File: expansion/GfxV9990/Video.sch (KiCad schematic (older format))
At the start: 1 part

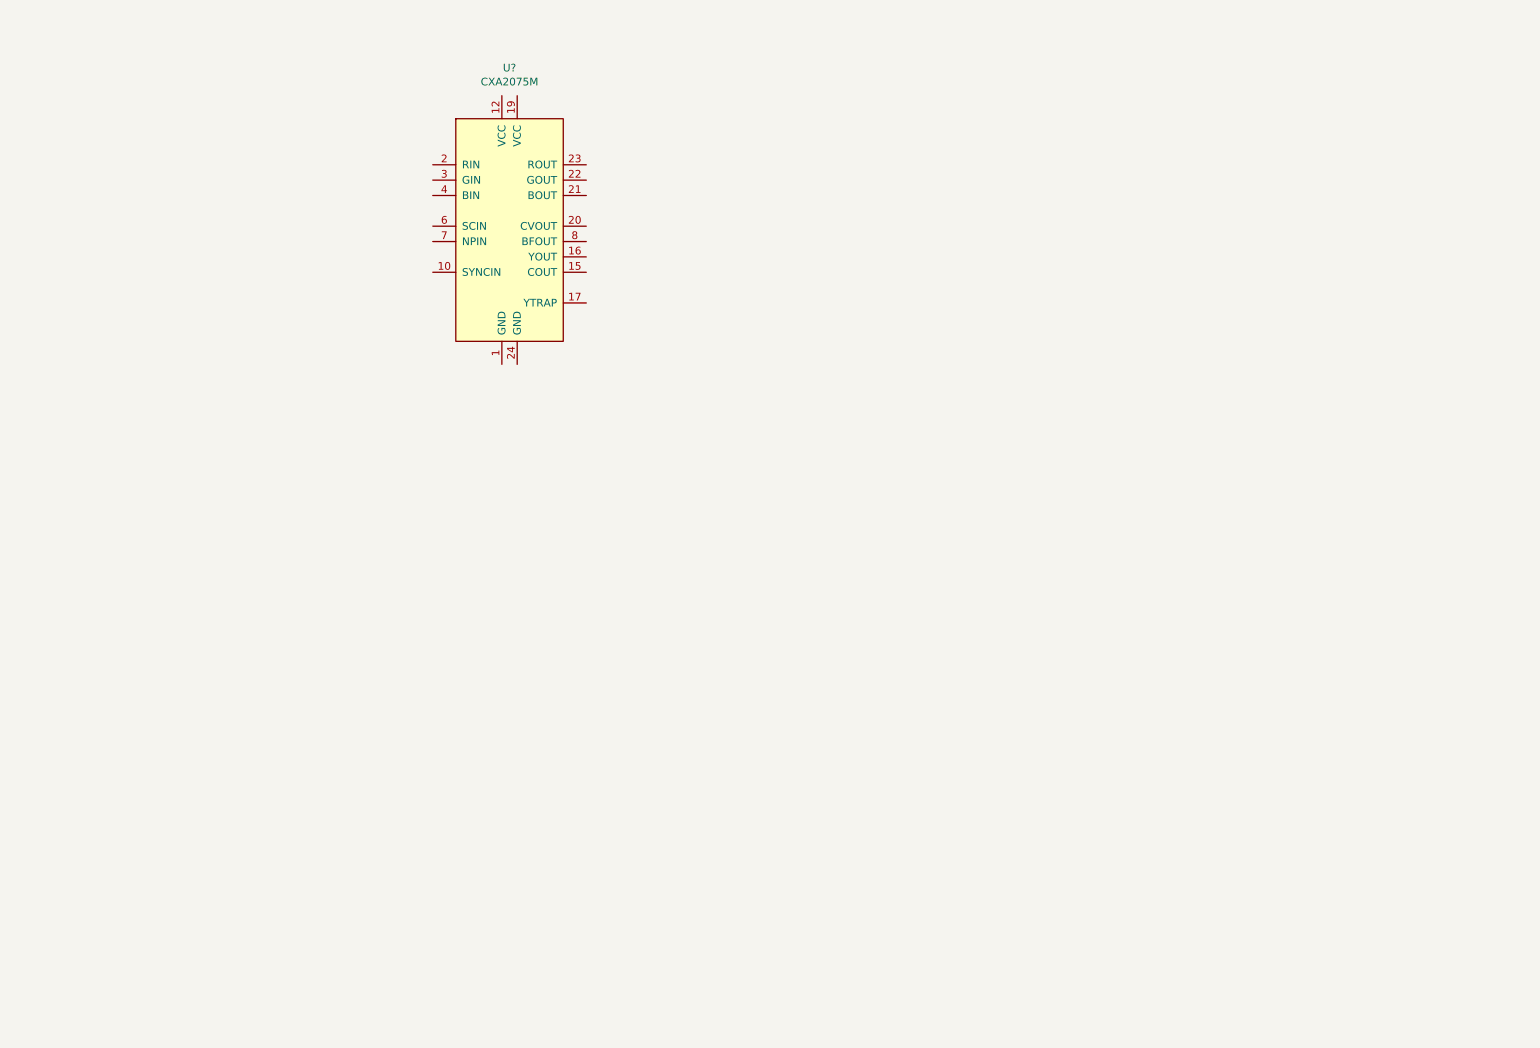
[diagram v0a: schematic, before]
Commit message: More additions to the V9990
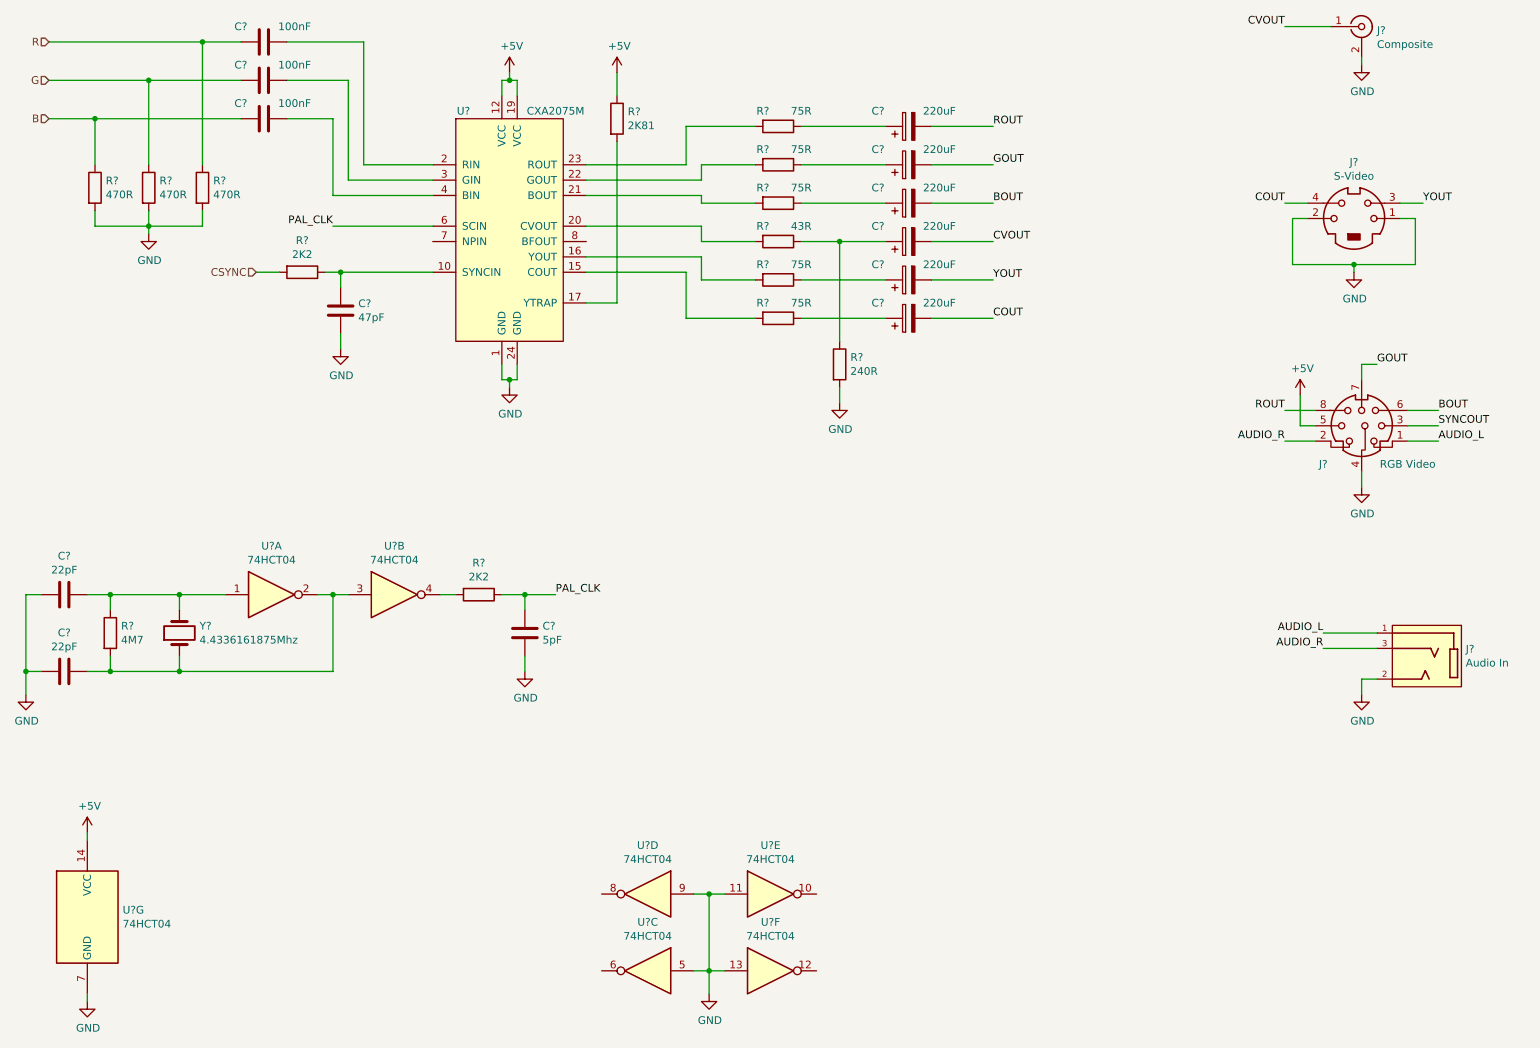
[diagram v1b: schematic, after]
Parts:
- added C? (x6): 220uF, symbol Device:CP
- added C?: 47pF, symbol Device:C
- added C? (x2): 22pF, symbol Device:C
- added C?: 5pF, symbol Device:C
- added C? (x3): 100nF, symbol Device:C
- added J?: RGB Video, symbol Connector:Mini-DIN-8
- added J?: S-Video, symbol Connector:Mini-DIN-4
- added J?: Composite, symbol Connector:Conn_Coaxial
- added J?: Audio In, SWITCHCRAFT_35RAPC2BHN2, symbol Ddraig:35RAPC2BHN2
- added R?: 2K81, symbol Device:R
- added R? (x5): 75R, symbol Device:R
- added R?: 43R, symbol Device:R
- added R?: 240R, symbol Device:R
- added R? (x2): 2K2, symbol Device:R
- added R?: 4M7, symbol Device:R
- added R? (x3): 470R, symbol Device:R
- added U? (x7): 74HCT04, symbol 74xx:74HCT04
- added Y?: 4.4336161875Mhz, symbol Device:Crystal
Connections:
- net GND: now reaches U?.1 (GND)
- net GND: now also U?.24 (GND), C?.2, C?.2, C?.2, C?.2, J?.1, J?.2, J?.2, J?.2 (Ext), J?.4, R?.2, R?.2, R?.2, R?.2, U?.11, U?.13, U?.5, U?.7 (GND), U?.9
- net at U?.10 (SYNCIN): now also C?.1, R?.1
- net +5V: now reaches U?.12 (VCC)
- net +5V: now also U?.19 (VCC), J?.5, R?.1, U?.14 (VCC)
- net at U?.15 (COUT): now also R?.2
- net at U?.16 (YOUT): now also R?.2
- net at U?.17 (YTRAP): now also R?.2
- net at U?.2 (RIN): now also C?.1
- net at U?.20 (CVOUT): now also R?.2
- net at U?.21 (BOUT): now also R?.2
- net at U?.22 (GOUT): now also R?.2
- net at U?.23 (ROUT): now also R?.2
- net at U?.3 (GIN): now also C?.1
- net at U?.4 (BIN): now also C?.1
- net PAL_CLK: now reaches U?.6 (SCIN)
- net PAL_CLK: now also C?.1, R?.1
- new net: C?.1, R?.1 (x5)
- new net: C?.1, R?.1, R?.1
- new net: C?.1, R?.1, U?.1, Y?.2
- new net: C?.1, R?.2, U?.2, U?.3, Y?.1
- new net: R?.2, U?.4
- new net AUDIO_L: J?.1, J?.1
- new net AUDIO_R: J?.2, J?.3
- new net B: C?.2, R?.1
- new net BOUT: C?.2, J?.6
- new net COUT: C?.2, J?.4
- new net CSYNC: R?.2
- new net CVOUT: C?.2, J?.1 (In)
- new net G: C?.2, R?.1
- new net GOUT: C?.2, J?.7
- new net R: C?.2, R?.1
- new net ROUT: C?.2, J?.8
- new net SYNCOUT: J?.3
- new net YOUT: C?.2, J?.3

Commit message: Added V9958 board
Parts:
- added C18: 220uF, symbol Device:CP
- added Q1: 2N3904, Package_TO_SOT_THT:TO-92_Inline, symbol Transistor_BJT:2N3904
- added R23, R24: R, symbol Device:R
- added R25: 220R, symbol Device:R
- J6: renamed from J?; footprint SWITCHCRAFT_35RAPC2BHN2 -> Ddraig:SWITCHCRAFT_35RAPC2BHN2
- gave numbers to parts that had none: 33
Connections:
- net +5V: now also Q1.3 (C)
- net CSYNC: now also R23.2
- net GND: now also R24.2
- net SYNCOUT: now also R25.1
- new net: Q1.2 (B), R23.1
- new net: C18.1, Q1.1 (E), R24.1
- new net: C18.2, R25.2
- no-connect marks 0 -> 6

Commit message: Added Eth8019 and updated page description for all projects
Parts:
- added C? (x3): 100nF, symbol Device:C
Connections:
- net +5V: now also C?.1, C?.1, C?.1
- net GND: now also C?.2, C?.2, C?.2
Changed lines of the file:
@@
 Wire Wire Line
 	8250 5150 8150 5150
+$Comp
+L Device:C C?
+U 1 1 60F7C479
+P 3400 6850
+F 0 "C?" H 3515 6896 50  0000 L CNN
+F 1 "100nF" H 3515 6805 50  0000 L CNN
+F 2 "" H 3438 6700 50  0001 C CNN
+F 3 "~" H 3400 6850 50  0001 C CNN
+	1    3400 6850
+	1    0    0    -1
+$EndComp
+$Comp
+L Device:C C?
+U 1 1 60F7C47F
+P 3850 6850
+F 0 "C?" H 3965 6896 50  0000 L CNN
+F 1 "100nF" H 3965 6805 50  0000 L CNN
+F 2 "" H 3888 6700 50  0001 C CNN
+F 3 "~" H 3850 6850 50  0001 C CNN
+	1    3850 6850
+	1    0    0    -1
+$EndComp
+$Comp
+L Device:C C?
+U 1 1 60F7C485
+P 2900 6850
+F 0 "C?" H 3015 6896 50  0000 L CNN
+F 1 "100nF" H 3015 6805 50  0000 L CNN
+F 2 "" H 2938 6700 50  0001 C CNN
+F 3 "~" H 2900 6850 50  0001 C CNN
+	1    2900 6850
+	1    0    0    -1
+$EndComp
+$Comp
+L power:GND #PWR?
+U 1 1 60F7C48B
+P 3400 7150
+F 0 "#PWR?" H 3400 6900 50  0001 C CNN
+F 1 "GND" H 3405 6977 50  0000 C CNN
+F 2 "" H 3400 7150 50  0001 C CNN
+F 3 "" H 3400 7150 50  0001 C CNN
+	1    3400 7150
+	1    0    0    -1
+$EndComp
+$Comp
+L power:+5V #PWR?
+U 1 1 60F7C491
+P 3400 6500
+F 0 "#PWR?" H 3400 6350 50  0001 C CNN
+F 1 "+5V" H 3415 6673 50  0000 C CNN
+F 2 "" H 3400 6500 50  0001 C CNN
+F 3 "" H 3400 6500 50  0001 C CNN
+	1    3400 6500
+	1    0    0    -1
+$EndComp
+Wire Wire Line
+	2900 6700 2900 6600
+Wire Wire Line
+	2900 6600 3400 6600
+Wire Wire Line
+	3850 6600 3850 6700
+Wire Wire Line
+	3400 6700 3400 6600
+Connection ~ 3400 6600
+Wire Wire Line
+	3400 6600 3850 6600
+Wire Wire Line
+	3400 6600 3400 6500
+Wire Wire Line
+	2900 7000 2900 7100
+Wire Wire Line
+	2900 7100 3400 7100
+Wire Wire Line
+	3850 7100 3850 7000
+Wire Wire Line
+	3400 7000 3400 7100
+Connection ~ 3400 7100
+Wire Wire Line
+	3400 7100 3850 7100
+Wire Wire Line
+	3400 7150 3400 7100
 $EndSCHEMATC

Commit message: Started work on V9990 PCB layout
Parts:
- C13: renamed from C5; footprint (none) -> Capacitor_SMD:C_0805_2012Metric
- C14: renamed from C6; footprint (none) -> Capacitor_SMD:C_0805_2012Metric
- C15: renamed from C7; footprint (none) -> Capacitor_SMD:C_0805_2012Metric
- C16: renamed from C8; footprint (none) -> Capacitor_SMD:C_0805_2012Metric
- C17: renamed from C9; footprint (none) -> Capacitor_SMD:C_0805_2012Metric
- C18, C20, C21: renamed from C?; footprint (none) -> Capacitor_SMD:C_0805_2012Metric
- C19: renamed from C10; footprint (none) -> Capacitor_SMD:C_0805_2012Metric
- C22: renamed from C11; footprint (none) -> Capacitor_SMD:C_0805_2012Metric
- C23: renamed from C12; footprint (none) -> Capacitor_SMD:CP_Elec_6.3x5.8
- C24: renamed from C13; footprint (none) -> Capacitor_SMD:CP_Elec_6.3x5.8
- C25: renamed from C14; footprint (none) -> Capacitor_SMD:CP_Elec_6.3x5.8
- C26: renamed from C15; footprint (none) -> Capacitor_SMD:CP_Elec_6.3x5.8
- C27: renamed from C16; footprint (none) -> Capacitor_SMD:CP_Elec_6.3x5.8
- C28: renamed from C17; footprint (none) -> Capacitor_SMD:CP_Elec_6.3x5.8
- C29: renamed from C18; footprint (none) -> Capacitor_SMD:CP_Elec_6.3x5.8
- J3: footprint (none) -> Ddraig:TE_5749181-1
- J4: footprint (none) -> Ddraig:KLPX0848A2RG
- J5: footprint (none) -> Ddraig:TE_57492681
- R10: renamed from R11; footprint (none) -> Inductor_SMD:L_0805_2012Metric
- R11: renamed from R12; footprint (none) -> Inductor_SMD:L_0805_2012Metric
- R12: renamed from R13; footprint (none) -> Inductor_SMD:L_0805_2012Metric
- R13: renamed from R14; footprint (none) -> Inductor_SMD:L_0805_2012Metric
- R14: renamed from R15; footprint (none) -> Inductor_SMD:L_0805_2012Metric
- R15: renamed from R16; footprint (none) -> Inductor_SMD:L_0805_2012Metric
- R16: renamed from R17; footprint (none) -> Inductor_SMD:L_0805_2012Metric
- R17: renamed from R18; footprint (none) -> Inductor_SMD:L_0805_2012Metric
- R18: renamed from R19; footprint (none) -> Inductor_SMD:L_0805_2012Metric
- R19: renamed from R20; footprint (none) -> Inductor_SMD:L_0805_2012Metric
- R20: renamed from R21; footprint (none) -> Inductor_SMD:L_0805_2012Metric
- R21: renamed from R22; footprint (none) -> Inductor_SMD:L_0805_2012Metric
- R22: renamed from R23; value R -> 1K; footprint (none) -> Inductor_SMD:L_0805_2012Metric
- R23: renamed from R24; value R -> 100R; footprint (none) -> Inductor_SMD:L_0805_2012Metric
- R24: renamed from R25; footprint (none) -> Inductor_SMD:L_0805_2012Metric
- R8: renamed from R9; footprint (none) -> Inductor_SMD:L_0805_2012Metric
- R9: renamed from R10; footprint (none) -> Inductor_SMD:L_0805_2012Metric
- U6: footprint (none) -> Package_SO:SO-14_5.3x10.2mm_P1.27mm
- Y2: footprint (none) -> Crystal:Crystal_HC50_Vertical

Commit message: Working on video board
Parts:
- removed Q1: 2N3904, Package_TO_SOT_THT:TO-92_Inline, symbol Transistor_BJT:2N3904
- added Q1: BC817, Package_TO_SOT_SMD:SOT-23, symbol Transistor_BJT:BC817
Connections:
- net +5V: now also Q1.3 (C)
- net at R22.1: now also Q1.1 (B)
- net at C29.1, R23.1: now also Q1.2 (E)
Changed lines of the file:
@@
-$EndComp
-$Comp
-L Transistor_BJT:2N3904 Q1
-U 1 1 60EAD7FF
-P 7000 4750
-F 0 "Q1" H 7190 4796 50  0000 L CNN
-F 1 "2N3904" H 7190 4705 50  0000 L CNN
-F 2 "Package_TO_SOT_THT:TO-92_Inline" H 7200 4675 50  0001 L CIN
-F 3 "https://www.onsemi.com/pub/Collateral/2N3903-D.PDF" H 7000 4750 50  0001 L CNN
-	1    7000 4750
-	1    0    0    -1
 $EndComp
 $Comp
@@
 Wire Wire Line
 	3400 7150 3400 7100
+$Comp
+L Transistor_BJT:BC817 Q1
+U 1 1 60DD58F4
+P 7000 4750
+F 0 "Q1" H 7191 4796 50  0000 L CNN
+F 1 "BC817" H 7191 4705 50  0000 L CNN
+F 2 "Package_TO_SOT_SMD:SOT-23" H 7200 4675 50  0001 L CIN
+F 3 "https://www.onsemi.com/pub/Collateral/BC818-D.pdf" H 7000 4750 50  0001 L CNN
+	1    7000 4750
+	1    0    0    -1
+$EndComp
 $EndSCHEMATC
